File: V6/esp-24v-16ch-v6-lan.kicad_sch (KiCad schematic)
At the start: 28 parts, among them J3 ETHERNET, U5 LAN8710A

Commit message: V6 is up
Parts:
- removed C18, C24: 10uF/10V, Tales:C_0603_1608Metric, symbol Device:C_Small
- added C20, C21: 10uF/25V, Tales:C_0805_2012Metric, symbol Device:C_Small
- J8: renamed from J3; footprint Tales:RJ45_HanRun_HR911105A -> Tales:RJ45_HanRun_HR915340A; symbol Tales:RJ45_HanRun_HR911105A -> Tales:RJ45_HanRun_HR915340A
- R30: renamed from R28; Package 0402/1005 -> (none)
- renumbered C26 to C18, C25 to C19, C19 to C22, C20 to C23, C21 to C24, C22 to C25, C23 to C26, R34 to R20, R20 to R21, R35 to R22, R21 to R23, R22 to R24, R23 to R25, R24 to R26, R25 to R27, R26 to R28, R27 to R29, R29 to R31, R30 to R32, R32 to R33, R31 to R34, R33 to R35
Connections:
- net +3V3A: no longer R20.1
- net +3V3LAN: now also R20.1, C21.1
- net ETHLEDYA: now also J8.11; no longer J8.12
- net GND: now also J8.12, C20.2, C21.2; no longer J8.11
- net PHYNRST: now also C20.1

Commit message: addressing the PHY power rails
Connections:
- net ETHLEDGA: now also J8.11, R22.2; no longer J8.9, R20.2
- net ETHLEDYA: now also J8.9, R20.2; no longer J8.11, R22.2
- net ETHLEDGK renamed ETHLEDYK
- net ETHLEDY renamed ETHLEDG
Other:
- note added: "GREEN LED: LNK/ACT YELLOW LED: SPEED, ON AT 100Mbps"
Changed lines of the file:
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@@
 		)
 	)
+	(text "GREEN LED: LNK/ACT\nYELLOW LED: SPEED,\nON AT 100Mbps"
+		(exclude_from_sim no)
+		(at 55.88 130.81 0)
+		(effects
+			(font
+				(size 1.27 1.27)
+			)
+			(justify left)
+		)
+	)
 	(text "RESISTORS: 62,5mW WHERE NOT SPECIFIED"
 		(exclude_from_sim no)
@@
 		)
 	)
-	(label "ETHLEDY"
+	(label "ETHLEDG"
 		(at 199.39 81.28 0)
 		(effects
@@
 		)
 	)
-	(label "ETHLEDYA"
+	(label "ETHLEDGA"
 		(at 50.8 134.62 90)
 		(effects
@@
 		)
 	)
-	(label "ETHLEDGA"
+	(label "ETHLEDYA"
 		(at 43.18 138.43 90)
 		(effects
@@
 		)
 	)
-	(label "ETHLEDGK"
+	(label "ETHLEDYK"
 		(at 199.39 83.82 0)
 		(effects
@@
 		(dnp no)
 		(property "Reference" "D7"
-			(at 252.73 69.85 0)
+			(at 252.73 68.58 0)
 			(show_name no)
 			(do_not_autoplace no)
@@
 		)
 		(property "Value" "ESDS314DBV"
-			(at 252.73 72.39 0)
+			(at 252.73 71.12 0)
 			(show_name no)
 			(do_not_autoplace no)
@@
 		)
 		(property "LCSC Part #" "C1847859"
-			(at 252.73 82.55 0)
-			(hide yes)
+			(at 252.73 73.66 0)
 			(show_name no)
 			(do_not_autoplace no)

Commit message: Revising power rails
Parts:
- removed C21: 10uF/25V, Tales:C_0805_2012Metric, symbol Device:C_Small
- renumbered C18 to C20, C19 to C21, C20 to C22, C22 to C23, C23 to C24, C24 to C25, C25 to C26, C26 to C27, R25 to R20, R20 to R24, R24 to R25
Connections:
- net +3V3A: now also J8.9
- net +3V3LAN: no longer R24.1
- net ETHLEDGA: now also U5.3 (LED1/~{REGOFF}); no longer R22.2
- net ETHLEDYK: now also R24.1; no longer U5.2 (LED2/~{INTSEL})
- net GND: now also R22.2; no longer J8.12
- net ETHLEDG renamed ETHLEDGK
- net ETHLEDGK: now also J8.12; no longer U5.3 (LED1/~{REGOFF})
- net ETHLEDYA renamed ETHLEDY
- net ETHLEDY: now also U5.2 (LED2/~{INTSEL}); no longer J8.9
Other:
- note added: "MODE[2:0]=111 ALL CAPABLE AUTONEG ENABLED"
- note added: "PHYAD[2:0]=000 PHY ADRESS 0X00"
- note added: "RMIISEL=1 RMII MODE"
- moved on the sheet: C22, R20, R21, R22, R23, R24, R25, R26, R27, R28, R29, R30

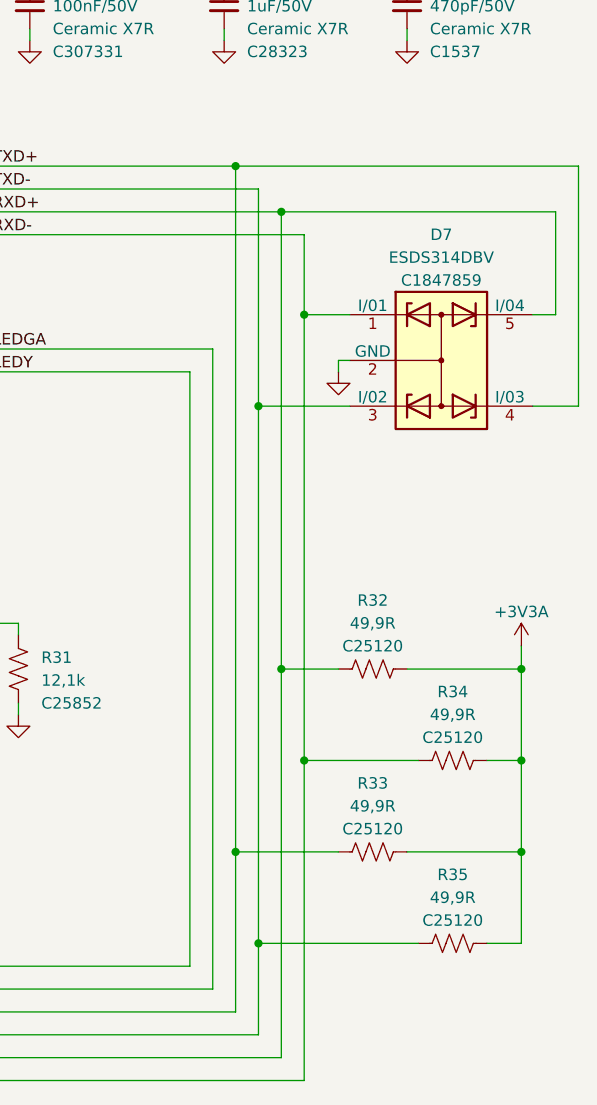
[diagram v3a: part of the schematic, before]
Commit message: ESP32 repositioned for shorter PHY traces.
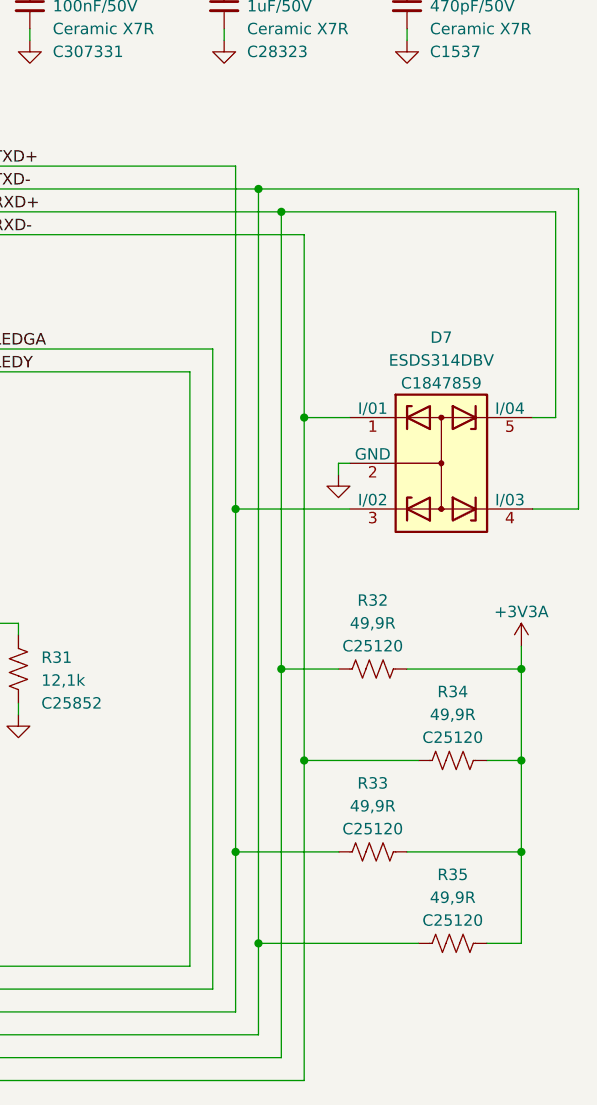
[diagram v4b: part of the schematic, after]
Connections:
- net ETHTXD+: now also D7.3 (I/02); no longer D7.4 (I/03)
- net ETHTXD-: now also D7.4 (I/03); no longer D7.3 (I/02)
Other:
- moved on the sheet: D7
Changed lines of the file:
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@@
 	)
 	(junction
-		(at 232.41 147.32)
-		(diameter 0)
-		(color 0 0 0 0)
-	)
-	(junction
 		(at 234.95 116.84)
 		(diameter 0)
@@
 	)
 	(junction
-		(at 229.87 60.96)
-		(diameter 0)
-		(color 0 0 0 0)
-	)
-	(junction
 		(at 73.66 160.02)
 		(diameter 0)
@@
 	)
 	(junction
-		(at 237.49 127)
-		(diameter 0)
-		(color 0 0 0 0)
-	)
-	(junction
 		(at 154.94 31.75)
 		(diameter 0)
@@
 	)
 	(junction
+		(at 232.41 63.5)
+		(diameter 0)
+		(color 0 0 0 0)
+	)
+	(junction
 		(at 59.69 38.1)
 		(diameter 0)
@@
 	)
 	(junction
-		(at 80.01 81.28)
+		(at 229.87 99.06)
 		(diameter 0)
 		(color 0 0 0 0)
 	)
 	(junction
-		(at 232.41 87.63)
+		(at 80.01 81.28)
 		(diameter 0)
 		(color 0 0 0 0)
@@
 	)
 	(junction
+		(at 232.41 147.32)
+		(diameter 0)
+		(color 0 0 0 0)
+	)
+	(junction
 		(at 48.26 104.14)
 		(diameter 0)
@@
 	)
 	(junction
-		(at 237.49 77.47)
+		(at 237.49 127)
+		(diameter 0)
+		(color 0 0 0 0)
+	)
+	(junction
+		(at 237.49 88.9)
 		(diameter 0)
 		(color 0 0 0 0)
@@
 	(wire
 		(pts
-			(xy 232.41 87.63) (xy 232.41 147.32)
+			(xy 232.41 63.5) (xy 232.41 147.32)
 		)
 		(stroke
@@
 	(wire
 		(pts
-			(xy 241.3 82.55) (xy 242.57 82.55)
+			(xy 241.3 93.98) (xy 242.57 93.98)
 		)
 		(stroke
@@
 	(wire
 		(pts
+			(xy 232.41 63.5) (xy 267.97 63.5)
+		)
+		(stroke
+			(width 0)
+			(type default)
+		)
+	)
+	(wire
+		(pts
 			(xy 228.6 31.75) (xy 248.92 31.75)
 		)
@@
 	(wire
 		(pts
-			(xy 237.49 77.47) (xy 237.49 127)
+			(xy 237.49 88.9) (xy 237.49 127)
 		)
 		(stroke
@@
 	(wire
 		(pts
+			(xy 229.87 99.06) (xy 242.57 99.06)
+		)
+		(stroke
+			(width 0)
+			(type default)
+		)
+	)
+	(wire
+		(pts
 			(xy 48.26 38.1) (xy 59.69 38.1)
 		)
@@
 	(wire
 		(pts
-			(xy 262.89 77.47) (xy 265.43 77.47)
+			(xy 262.89 88.9) (xy 265.43 88.9)
 		)
 		(stroke
@@
 	(wire
 		(pts
-			(xy 267.97 87.63) (xy 267.97 60.96)
+			(xy 267.97 99.06) (xy 267.97 63.5)
 		)
 		(stroke
@@
 	(wire
 		(pts
+			(xy 229.87 99.06) (xy 229.87 137.16)
+		)
+		(stroke
+			(width 0)
+			(type default)
+		)
+	)
+	(wire
+		(pts
 			(xy 83.82 152.4) (xy 227.33 152.4)
 		)
@@
 	(wire
 		(pts
-			(xy 237.49 68.58) (xy 237.49 77.47)
+			(xy 237.49 68.58) (xy 237.49 88.9)
 		)
 		(stroke
@@
 	(wire
 		(pts
-			(xy 265.43 77.47) (xy 265.43 66.04)
+			(xy 265.43 88.9) (xy 265.43 66.04)
 		)
 		(stroke
@@
 	(wire
 		(pts
-			(xy 241.3 83.82) (xy 241.3 82.55)
+			(xy 241.3 95.25) (xy 241.3 93.98)
 		)
 		(stroke
@@
 	(wire
 		(pts
-			(xy 267.97 60.96) (xy 229.87 60.96)
-		)
-		(stroke
-			(width 0)
-			(type default)
-		)
-	)
-	(wire
-		(pts
 			(xy 248.92 45.72) (xy 248.92 46.99)
 		)
@@
 	(wire
 		(pts
-			(xy 237.49 77.47) (xy 242.57 77.47)
+			(xy 237.49 88.9) (xy 242.57 88.9)
 		)
 		(stroke
@@
 	(wire
 		(pts
-			(xy 232.41 87.63) (xy 242.57 87.63)
-		)
-		(stroke
-			(width 0)
-			(type default)
-		)
-	)
-	(wire
-		(pts
 			(xy 179.07 38.1) (xy 184.15 38.1)
 		)
@@
 	(wire
 		(pts
-			(xy 229.87 60.96) (xy 229.87 137.16)
+			(xy 229.87 60.96) (xy 229.87 99.06)
 		)
 		(stroke
@@
 	(wire
 		(pts
-			(xy 232.41 63.5) (xy 232.41 87.63)
-		)
-		(stroke
-			(width 0)
-			(type default)
-		)
-	)
-	(wire
-		(pts
 			(xy 73.66 160.02) (xy 73.66 149.86)
 		)
@@
 	(wire
 		(pts
-			(xy 262.89 87.63) (xy 267.97 87.63)
+			(xy 262.89 99.06) (xy 267.97 99.06)
 		)
 		(stroke
@@
 	(symbol
 		(lib_id "power:GND")
-		(at 241.3 83.82 0)
+		(at 241.3 95.25 0)
 		(unit 1)
 		(body_style 1)
@@
 		(dnp no)
 		(property "Reference" "#PWR068"
-			(at 241.3 90.17 0)
+			(at 241.3 101.6 0)
 			(hide yes)
 			(show_name no)
@@
 		)
 		(property "Value" "GND"
-			(at 241.427 88.2142 0)
+			(at 241.427 99.6442 0)
 			(hide yes)
 			(show_name no)
@@
 		)
 		(property "Footprint" ""
-			(at 241.3 83.82 0)
+			(at 241.3 95.25 0)
 			(hide yes)
 			(show_name no)
@@
 		)
 		(property "Datasheet" ""
-			(at 241.3 83.82 0)
+			(at 241.3 95.25 0)
 			(hide yes)
 			(show_name no)
@@
 		)
 		(property "Description" "Power symbol creates a global label with name \"GND\" , ground"
-			(at 241.3 83.82 0)
+			(at 241.3 95.25 0)
 			(hide yes)
 			(show_name no)
@@
 	(symbol
 		(lib_id "Tales:ESDS314DBV")
-		(at 252.73 82.55 0)
+		(at 252.73 93.98 0)
 		(unit 1)
 		(body_style 1)
@@
 		(dnp no)
 		(property "Reference" "D7"
-			(at 252.73 68.58 0)
+			(at 252.73 80.01 0)
 			(show_name no)
 			(do_not_autoplace no)
@@
 		)
 		(property "Value" "ESDS314DBV"
-			(at 252.73 71.12 0)
+			(at 252.73 82.55 0)
 			(show_name no)
 			(do_not_autoplace no)
@@
 		)
 		(property "Footprint" "Tales:SOT-23-5"
-			(at 254 91.44 0)
+			(at 254 102.87 0)
 			(hide yes)
 			(show_name no)
@@
 		)
 		(property "Datasheet" ""
-			(at 252.73 82.55 0)
+			(at 252.73 93.98 0)
 			(hide yes)
 			(show_name no)
@@
 		)
 		(property "Description" "Data-line surge and ESD protection diode array"
-			(at 252.73 82.55 0)
+			(at 252.73 93.98 0)
 			(hide yes)
 			(show_name no)
@@
 		)
 		(property "Vendor" "JLCPCB"
-			(at 252.73 82.55 0)
+			(at 252.73 93.98 0)
 			(hide yes)
 			(show_name no)
@@
 		)
 		(property "Case" "SOT-23-5"
-			(at 252.73 82.55 0)
+			(at 252.73 93.98 0)
 			(hide yes)
 			(show_name no)
@@
 		)
 		(property "JLCPCB BOM" "1"
-			(at 252.73 82.55 0)
+			(at 252.73 93.98 0)
 			(hide yes)
 			(show_name no)
@@
 		)
 		(property "LCSC Part #" "C1847859"
-			(at 252.73 73.66 0)
+			(at 252.73 85.09 0)
 			(show_name no)
 			(do_not_autoplace no)
@@
 		)
 		(property "Mfr" "Texas Instruments"
-			(at 252.73 82.55 0)
+			(at 252.73 93.98 0)
 			(hide yes)
 			(show_name no)
@@
 		)
 		(property "Mfr PN" "ESDS314DBVR"
-			(at 252.73 82.55 0)
+			(at 252.73 93.98 0)
 			(hide yes)
 			(show_name no)
@@
 		)
 		(property "Technology" ""
-			(at 252.73 82.55 0)
+			(at 252.73 93.98 0)
 			(hide yes)
 			(show_name no)
@@
 		)
 		(property "Vendor PN" "C1847859"
-			(at 252.73 82.55 0)
+			(at 252.73 93.98 0)
 			(hide yes)
 			(show_name no)

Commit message: Included test points
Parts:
- added TP13: VCDDR, TestPoint:TestPoint_Pad_D1.5mm, symbol Connector:TestPoint
- added TP14: RXD0, TestPoint:TestPoint_Pad_D1.5mm, symbol Connector:TestPoint
- added TP15: CLK, TestPoint:TestPoint_Pad_D1.5mm, symbol Connector:TestPoint
- added TP16: PHYEN, TestPoint:TestPoint_Pad_D1.5mm, symbol Connector:TestPoint
- R20, R21, R23, R25, R26, R27, R28, R29: value 2k2 -> 10k; LCSC Part # C25879 -> C25744; Mfr PN 0402WGF2201TCE -> 0402WGF1002TCE; Vendor PN C25879 -> C25744
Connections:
- net EMACCLK: now also TP15.1
- net EMACRXD0: now also TP14.1
- net PHYNRST: now also TP16.1
- net VCDDR: now also TP13.1

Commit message: Removed test points that didn't fit the PCB
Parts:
- TP13, TP14: now left out of the parts list
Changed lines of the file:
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@@
 		(body_style 1)
 		(exclude_from_sim no)
-		(in_bom yes)
-		(on_board yes)
+		(in_bom no)
+		(on_board no)
 		(in_pos_files yes)
 		(dnp yes)
@@
 		(body_style 1)
 		(exclude_from_sim no)
-		(in_bom yes)
-		(on_board yes)
+		(in_bom no)
+		(on_board no)
 		(in_pos_files yes)
 		(dnp yes)

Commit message: Correcting JLCPBC part number for J8 ethernet connector
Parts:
- J8: LCSC Part # C12074 -> C2760325; Mfr PN HR911105A -> HR915340A; Vendor PN C12074 -> C2760325
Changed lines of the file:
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@@
 			)
 		)
-		(property "LCSC Part #" "C12074"
+		(property "LCSC Part #" "C2760325"
 			(at 34.29 159.3849 0)
 			(show_name no)
@@
 			)
 		)
-		(property "Mfr PN" "HR911105A"
+		(property "Mfr PN" "HR915340A"
 			(at 48.26 154.94 0)
 			(hide yes)
@@
 			)
 		)
-		(property "Vendor PN" "C12074"
+		(property "Vendor PN" "C2760325"
 			(at 48.26 154.94 0)
 			(hide yes)

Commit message: Included a shunt resistor on the 5V rail, for measuring current during development.
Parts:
- renumbered TP13 to TP14, TP14 to TP15, TP15 to TP16, TP16 to TP17
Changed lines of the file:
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@@
 		(in_pos_files yes)
 		(dnp yes)
-		(property "Reference" "TP14"
+		(property "Reference" "TP15"
 			(at 128.27 66.04 0)
 			(show_name no)
@@
 			(project "esp-24v-16ch-v6"
 				(path "/2bc5a21a-1d79-419d-a592-6852cc07b00a/c76fc600-a423-4f14-bc69-e86c7c986b21"
-					(reference "TP14")
+					(reference "TP15")
 					(unit 1)
 				)
@@
 		(in_pos_files yes)
 		(dnp no)
-		(property "Reference" "TP16"
+		(property "Reference" "TP17"
 			(at 116.84 118.11 0)
 			(show_name no)
@@
 			(project "esp-24v-16ch-v6"
 				(path "/2bc5a21a-1d79-419d-a592-6852cc07b00a/c76fc600-a423-4f14-bc69-e86c7c986b21"
-					(reference "TP16")
+					(reference "TP17")
 					(unit 1)
 				)
@@
 		(in_pos_files yes)
 		(dnp no)
-		(property "Reference" "TP15"
+		(property "Reference" "TP16"
 			(at 58.42 91.44 0)
 			(show_name no)
@@
 			(project "esp-24v-16ch-v6"
 				(path "/2bc5a21a-1d79-419d-a592-6852cc07b00a/c76fc600-a423-4f14-bc69-e86c7c986b21"
-					(reference "TP15")
+					(reference "TP16")
 					(unit 1)
 				)
@@
 		(in_pos_files yes)
 		(dnp yes)
-		(property "Reference" "TP13"
+		(property "Reference" "TP14"
 			(at 247.65 20.32 0)
 			(show_name no)
@@
 			(project "esp-24v-16ch-v6"
 				(path "/2bc5a21a-1d79-419d-a592-6852cc07b00a/c76fc600-a423-4f14-bc69-e86c7c986b21"
-					(reference "TP13")
+					(reference "TP14")
 					(unit 1)
 				)
